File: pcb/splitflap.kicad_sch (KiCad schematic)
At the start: 37 parts, among them J1 Motor A, J10 Hall C, J11 Hall-D, J2 Motor B, J3 Motor C, J4 Motor D, J7 Barrel_Jack_Switch, J8 Hall A, J9 Hall B, SW1 A, SW2 B, SW3 IO0, SW4 RST, U1 ULN2003, U12 LM2596S-5, U2 ULN2003, U3 ESP32-DevKitC, U4 ULN2003

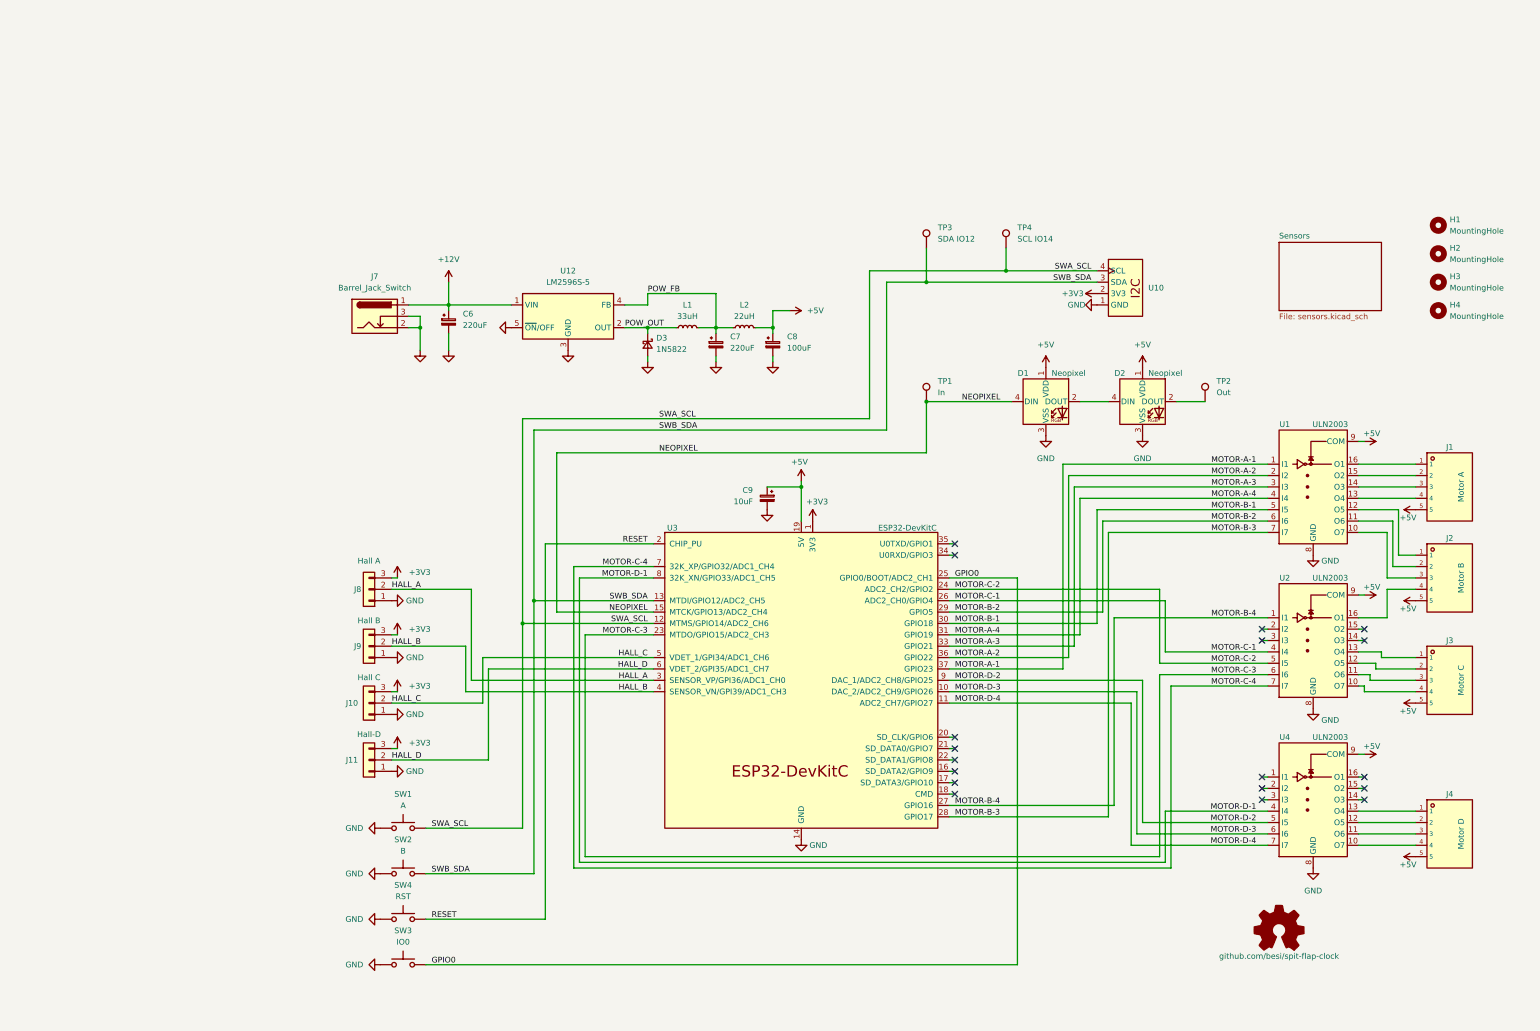
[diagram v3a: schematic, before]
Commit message: Rework 6
Added power flags to external power inputs. Fixed Motor connector pins from Unspecified to Passive, per KiCad fashion. Made the ERC pass without exclusions.

Added power decoupling to Hall sensor connectors and to the Neopixels.

Moved the IN test point for better probing accessibility. Test points use teardrop connections for integrity in face of probing.

Added a ground clip area for scope probes etc.

Added a 3D model of the pushbuttons.
Rework 6

Change revision to 1.2.
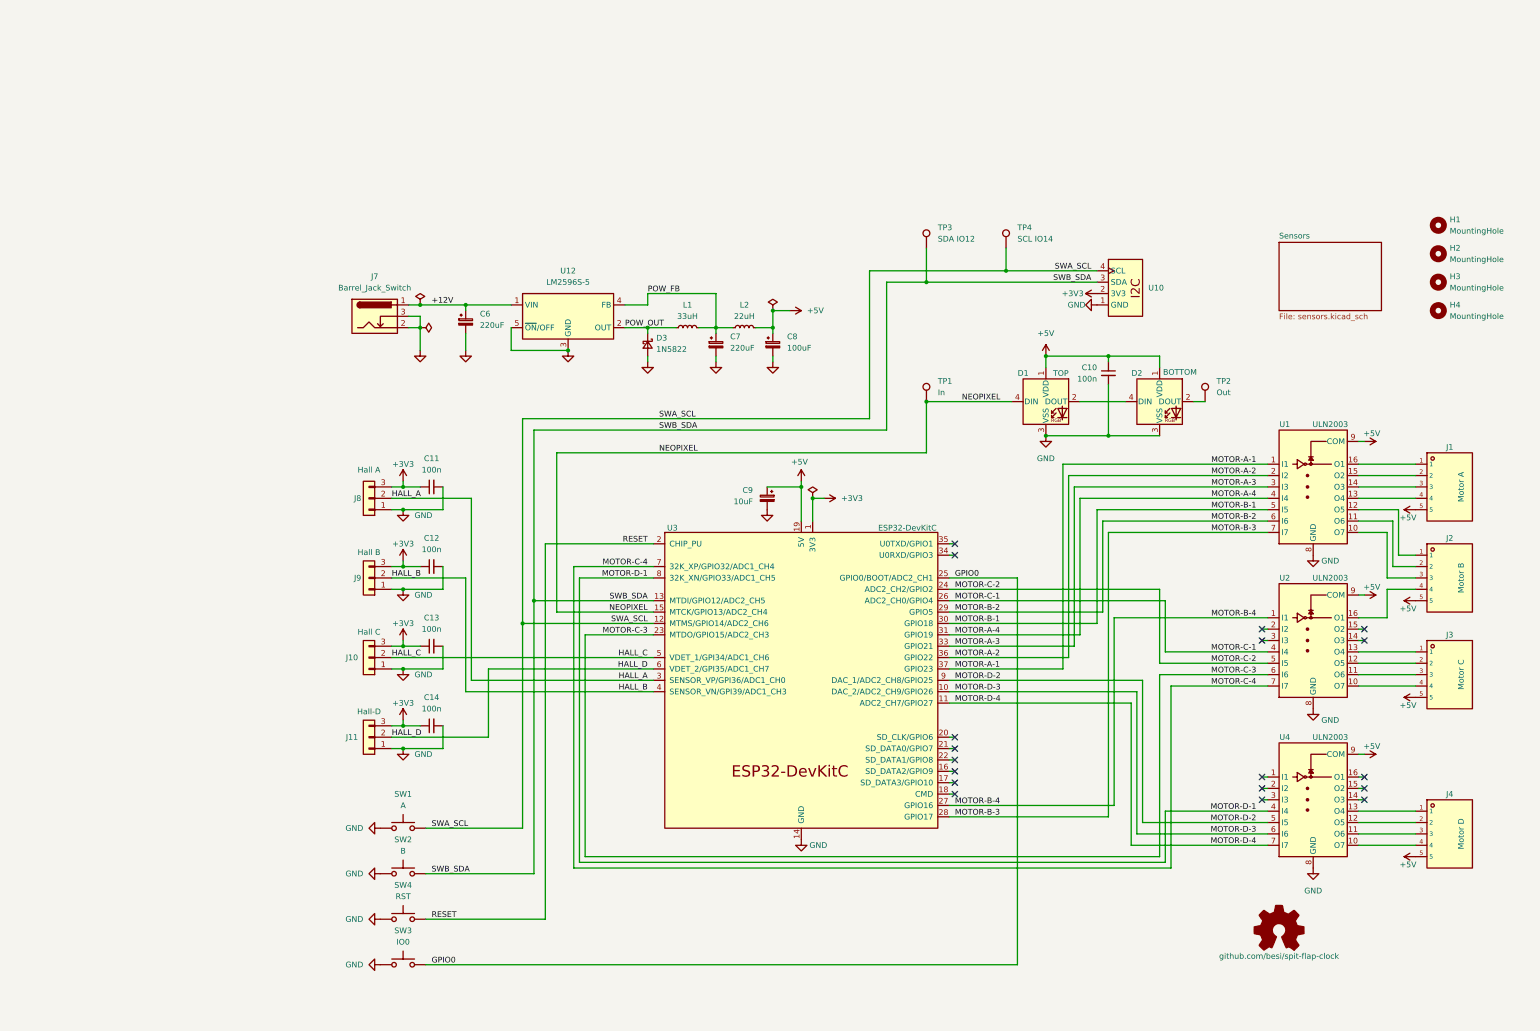
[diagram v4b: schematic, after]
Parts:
- added C10, C11, C12, C13, C14: 100n, Capacitor_SMD:C_0805_2012Metric_Pad1.18x1.45mm_HandSolder, symbol Device:C_Small
- D1: Label (none) -> TOP
- D2: Label (none) -> BOTTOM
- J1, J2, J3, J4: symbol B5B-XH-A_(LF)(SN):B5B-XH-A_(LF)(SN) -> jlc_symbols:B5B-XH-A_(LF)(SN)
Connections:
- net +3V3: now also C11.1, C12.1, C13.1, C14.1
- net +5V: now also C10.1
- net GND: now also C10.2, C11.2, C12.2, C13.2, C14.2
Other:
- moved on the sheet: C6, D2, J10, J11, J3, J8, J9

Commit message: Draft of v2 board to be imported in Fusion360
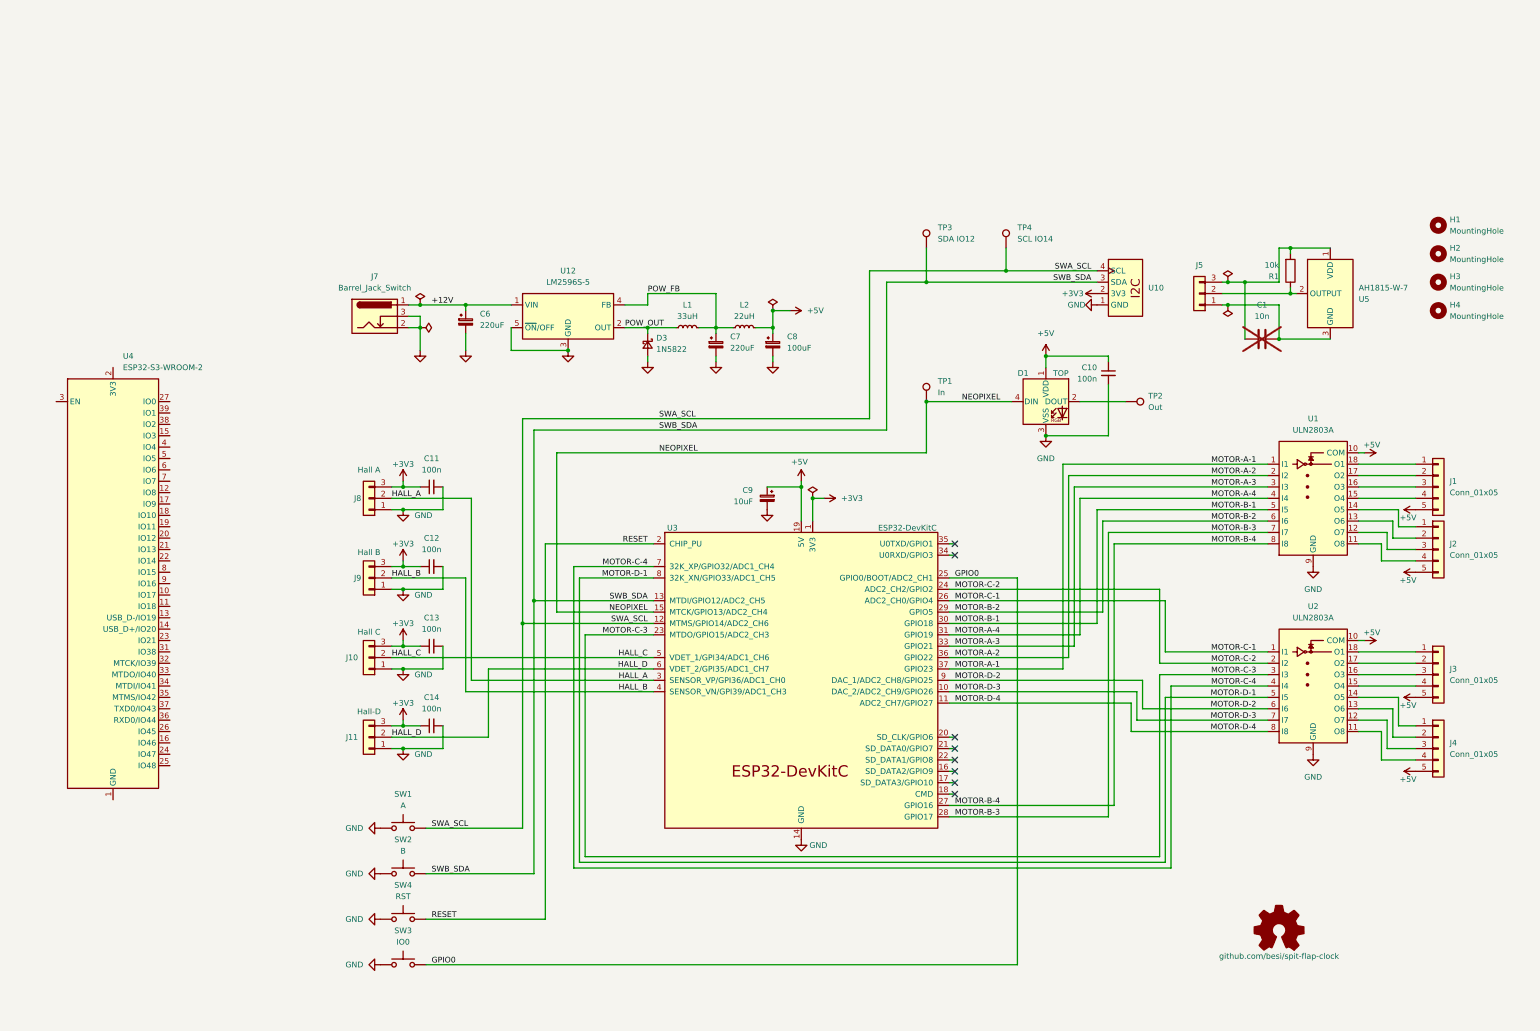
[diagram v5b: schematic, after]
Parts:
- removed D2: Neopixel, LED_SMD:LED_WS2812B_PLCC4_5.0x5.0mm_P3.2mm, symbol LED:WS2812B
- removed J1: Motor A, jlc_footprints:CONN-TH_B5B-XH-A-LF-SN, symbol jlc_symbols:B5B-XH-A_(LF)(SN)
- removed J2: Motor B, jlc_footprints:CONN-TH_B5B-XH-A-LF-SN, symbol jlc_symbols:B5B-XH-A_(LF)(SN)
- removed J3: Motor C, jlc_footprints:CONN-TH_B5B-XH-A-LF-SN, symbol jlc_symbols:B5B-XH-A_(LF)(SN)
- removed J4: Motor D, jlc_footprints:CONN-TH_B5B-XH-A-LF-SN, symbol jlc_symbols:B5B-XH-A_(LF)(SN)
- removed U1, U2, U4: ULN2003, Package_SO:SOIC-16_3.9x9.9mm_P1.27mm, symbol Transistor_Array:ULN2003
- added C1: 10n, symbol Device:C
- added J1, J2, J3, J4: Conn_01x05, Connector_JST:JST_XH_B5B-XH-A_1x05_P2.50mm_Vertical, symbol Connector_Generic:Conn_01x05
- added J5: Conn_01x03, Connector_PinHeader_2.54mm:PinHeader_1x03_P2.54mm_Vertical, symbol Connector_Generic:Conn_01x03
- added R1: 10k, Resistor_SMD:R_0805_2012Metric_Pad1.20x1.40mm_HandSolder, symbol Device:R
- added U1, U2: ULN2803A, Package_SO:SOP-18_7.495x11.515mm_P1.27mm, symbol Transistor_Array:ULN2803A
- added U4: ESP32-S3-WROOM-2, RF_Module:ESP32-S3-WROOM-2, symbol RF_Module:ESP32-S3-WROOM-2
- added U5: AH1815-W-7, Package_TO_SOT_SMD:SC-59_Handsoldering, symbol Sensor_Magnetic:AH1806-W
- J10, J11, J8, J9: footprint Connector_JST:JST_EH_B3B-EH-A_1x03_P2.50mm_Vertical -> Connector_JST:JST_XH_B3B-XH-A_1x03_P2.50mm_Vertical
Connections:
- net +5V: now also J1.5 (Pin_5), J2.5 (Pin_5), J3.5 (Pin_5), J4.5 (Pin_5), U1.10 (COM), U2.10 (COM)
- net GND: now also U1.9 (GND), U2.9 (GND)
- net MOTOR-A-1: now also U1.1 (I1)
- net MOTOR-A-2: now also U1.2 (I2)
- net MOTOR-A-3: now also U1.3 (I3)
- net MOTOR-A-4: now also U1.4 (I4)
- net MOTOR-B-1: now also U1.5 (I5)
- net MOTOR-B-2: now also U1.6 (I6)
- net MOTOR-B-3: now also U1.7 (I7)
- net MOTOR-B-4: now also U1.8 (I8)
- net MOTOR-C-1: now also U2.1 (I1)
- net MOTOR-C-2: now also U2.2 (I2)
- net MOTOR-C-3: now also U2.3 (I3)
- net MOTOR-C-4: now also U2.4 (I4)
- net MOTOR-D-1: now also U2.5 (I5)
- net MOTOR-D-2: now also U2.6 (I6)
- net MOTOR-D-3: now also U2.7 (I7)
- net MOTOR-D-4: now also U2.8 (I8)
- net at TP2.1: now also D1.2 (DOUT)
- new net: C1.1, J5.3 (Pin_3), R1.2, U5.1 (VDD)
- new net: J5.2 (Pin_2), R1.1, U5.2 (OUTPUT)
- new net: C1.2, J5.1 (Pin_1), U5.3 (GND)
- new net: J4.4 (Pin_4), U2.11 (O8)
- new net: J4.3 (Pin_3), U2.12 (O7)
- new net: J4.2 (Pin_2), U2.13 (O6)
- new net: J4.1 (Pin_1), U2.14 (O5)
- new net: J3.4 (Pin_4), U2.15 (O4)
- new net: J3.3 (Pin_3), U2.16 (O3)
- new net: J3.2 (Pin_2), U2.17 (O2)
- new net: J3.1 (Pin_1), U2.18 (O1)
- new net: J2.4 (Pin_4), U1.11 (O8)
- new net: J2.3 (Pin_3), U1.12 (O7)
- new net: J2.2 (Pin_2), U1.13 (O6)
- new net: J2.1 (Pin_1), U1.14 (O5)
- new net: J1.4 (Pin_4), U1.15 (O4)
- new net: J1.3 (Pin_3), U1.16 (O3)
- new net: J1.2 (Pin_2), U1.17 (O2)
- new net: J1.1 (Pin_1), U1.18 (O1)
- new net: U4.1 (GND), U4.40 (GND), U4.41 (GND)
- no-connect marks 18 -> 8
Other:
- removed sheet Sensors
- moved on the sheet: TP2

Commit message: V2 WIP
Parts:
- removed C7: 220uF, Capacitor_THT:CP_Radial_D10.0mm_P3.50mm, symbol Device:C_Polarized_Small
- removed D1: Neopixel, LED_SMD:LED_WS2812B_PLCC4_5.0x5.0mm_P3.2mm, symbol LED:WS2812B
- removed J5: Conn_01x03, Connector_PinHeader_2.54mm:PinHeader_1x03_P2.54mm_Vertical, symbol Connector_Generic:Conn_01x03
- removed TP1: In, TestPoint:TestPoint_Pad_D1.5mm, symbol Connector:TestPoint
- removed TP2: Out, TestPoint:TestPoint_Pad_D1.5mm, symbol Connector:TestPoint
- removed TP3: SDA IO12, TestPoint:TestPoint_Pad_D1.5mm, symbol Connector:TestPoint
- removed TP4: SCL IO14, TestPoint:TestPoint_Pad_D1.5mm, symbol Connector:TestPoint
- removed U3: ESP32-DevKitC, PCM_Espressif:ESP32-DevKitC, symbol espsbeat:ESP32-DevKitC
- added C15, C7: 100n, Capacitor_SMD:C_0805_2012Metric_Pad1.18x1.45mm_HandSolder, symbol Device:C_Small
- added C16, C3: 10u @ 16V, Capacitor_SMD:CP_Elec_4x5.7, symbol Device:C_Polarized_Small
- added C18: 1u, Capacitor_SMD:C_0805_2012Metric_Pad1.18x1.45mm_HandSolder, symbol Device:C_Small
- added C2, C4: 100uF, Capacitor_SMD:CP_Elec_5x5.3, symbol Device:C_Polarized_Small
- added C5: 220uF, Capacitor_SMD:CP_Elec_8x11.9, symbol Device:C_Polarized_Small
- added D1: SK6812MINI, LED_SMD:LED_SK6812MINI_PLCC4_3.5x3.5mm_P1.75mm, symbol LED:SK6812MINI
- added J5: Barrel_Jack_Switch, pj-060a:pj-060a, symbol Connector:Barrel_Jack_Switch
- added J6: USB_C_Receptacle_USB2.0_16P, Connector_USB:USB_C_Receptacle_GCT_USB4105-xx-A_16P_TopMnt_Horizontal, symbol Connector:USB_C_Receptacle_USB2.0_16P
- added M1: ~, 28byj:28byj, symbol 28byj:28byj
- added R2, R3: 5k1, Resistor_SMD:R_0603_1608Metric, symbol Device:R_Small
- added R4: 10k, Resistor_SMD:R_0603_1608Metric_Pad0.98x0.95mm_HandSolder, symbol Device:R
- added U3: DS18B20, Package_TO_SOT_THT:TO-92_Inline_Wide, symbol Sensor_Temperature:DS18B20
- added U6: UART, Connector_PinHeader_2.54mm:PinHeader_1x04_P2.54mm_Vertical, symbol ftdi-connector:TTL
- added U7: LD1117S33CTR, Package_TO_SOT_SMD:SOT-223-3_TabPin2, symbol Regulator_Linear:LD1117S33TR_SOT223
- added U8: DCF-77, dcf77:dcf77, symbol dcf77:dcf77
- C1: now fitted
- C10, C11, C12, C13, C14, J1, J2, J3, J4, J7, R1, U1, U2, U5: MPN (none) -> (none)
- C6: footprint Capacitor_THT:CP_Radial_D10.0mm_P3.50mm -> Capacitor_SMD:CP_Elec_8x11.9; MPN (none) -> A768KS227M1VLAE024
- C8: value 100uF -> 10u @ 16V; footprint Capacitor_THT:CP_Radial_D10.0mm_P3.50mm -> Capacitor_SMD:CP_Elec_4x5.7; MPN (none) -> 865080340001
- C9: value 10uF -> 10u @ 16V; footprint Capacitor_THT:CP_Radial_D5.0mm_P2.00mm -> Capacitor_SMD:CP_Elec_4x5.7; MPN (none) -> 865080340001
- D3: MPN (none) -> 1N5822
- H1, H2, H3, H4, OSHW1: MPN (none) -> (none); now not fitted
- J10, J11, J9: footprint Connector_JST:JST_XH_B3B-XH-A_1x03_P2.50mm_Vertical -> Connector_JST:JST_PH_B3B-PH-K_1x03_P2.00mm_Vertical; MPN (none) -> (none)
- J8: footprint Connector_JST:JST_XH_B3B-XH-A_1x03_P2.50mm_Vertical -> Connector_JST:JST_PH_B3B-PH-K_1x03_P2.00mm_Vertical
- L1: footprint Inductor_THT:L_Radial_D7.2mm_P3.00mm_Murata_1700 -> Inductor_SMD:L_APV_ANR6028; MPN (none) -> NR6028T330M
- L2: footprint Inductor_THT:L_Radial_D7.2mm_P3.00mm_Murata_1700 -> Inductor_SMD:L_APV_ANR5045; MPN (none) -> TYS5040220M-10
- SW1, SW2, SW4: MPN (none) -> 434133025816
- SW3: value IO0 -> Mode; MPN (none) -> 434133025816
- U10: footprint qwiic-adapter:qwiic-adapter -> Connector_JST:JST_SH_BM04B-SRSS-TB_1x04-1MP_P1.00mm_Vertical; MPN (none) -> BM04B-SRSS-TB
- U12: MPN (none) -> LM2596S-5.0
- U4: value ESP32-S3-WROOM-2 -> ESP32-S3-WROOM-1; footprint RF_Module:ESP32-S3-WROOM-2 -> RF_Module:ESP32-S3-WROOM-1; MPN (none) -> ESP32-S3-WROOM-1-N4
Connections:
- net +12V: now also J5.1
- net +3V3: now also C1.1, R1.2, U4.2 (3V3), U5.1 (VDD), C16.1, C2.1, C7.2, D1.4 (VDD), R4.2, U3.3 (V_{DD}), U6.4 (VDD), U7.2 (VO), U8.1 (VDD)
- net +5V: now also C10.2, C15.2, C3.1, C4.1, J6.A4 (VBUS), J6.A9 (VBUS), J6.B4 (VBUS), J6.B9 (VBUS), U7.3 (VI); no longer C10.1
- net GND: now also C1.2, C10.1, U4.1 (GND), U4.40 (GND), U4.41 (GND), U5.3 (GND), C15.1, C16.2, C18.1, C2.2, C3.2, C4.2, C5.2, C7.1, D1.2 (VSS), J5.2, U3.1 (GND), U6.1 (GND), U7.1 (GND), U8.2 (GND), U8.4 (~{EN}); no longer C10.2, J7.3
- net GPIO0: now also U4.27 (IO0)
- net HALL_A: now also R1.1, U4.11 (IO18), U5.2 (OUTPUT)
- net HALL_B: now also U4.25 (IO48)
- net HALL_C: now also U4.24 (IO47)
- net HALL_D: now also U4.20 (IO12)
- net MOTOR-A-1: now also U4.39 (IO1)
- net MOTOR-A-2: now also U4.38 (IO2)
- net MOTOR-A-3: now also U4.35 (MTMS/IO42)
- net MOTOR-A-4: now also U4.34 (MTDI/IO41)
- net MOTOR-B-1: now also U4.33 (MTDO/IO40)
- net MOTOR-B-2: now also U4.32 (MTCK/IO39)
- net MOTOR-B-3: now also U4.31 (IO38)
- net MOTOR-B-4: now also U4.6 (IO6)
- net MOTOR-C-1: now also U4.21 (IO13)
- net MOTOR-C-2: now also U4.22 (IO14)
- net MOTOR-C-3: now also U4.23 (IO21)
- net MOTOR-C-4: now also U4.19 (IO11)
- net MOTOR-D-1: now also U4.18 (IO10)
- net MOTOR-D-2: now also U4.17 (IO9)
- net MOTOR-D-3: now also U4.15 (IO3)
- net MOTOR-D-4: now also U4.12 (IO8)
- net POW_FB: now also C5.1
- net RESET: now also U4.3 (EN), C18.2, R4.1
- net SWA_SCL: now also U4.10 (IO17)
- net SWB_SDA: now also U4.9 (IO16)
- net MOUT-D4: now reaches J4.4 (Pin_4), U2.11 (O8)
- net MOUT-D3: now reaches J4.3 (Pin_3), U2.12 (O7)
- net MOUT-D2: now reaches J4.2 (Pin_2), U2.13 (O6)
- net MOUT-D1: now reaches J4.1 (Pin_1), U2.14 (O5)
- net MOUT-C4: now reaches J3.4 (Pin_4), U2.15 (O4)
- net MOUT-C3: now reaches J3.3 (Pin_3), U2.16 (O3)
- net MOUT-C2: now reaches J3.2 (Pin_2), U2.17 (O2)
- net MOUT-C1: now reaches J3.1 (Pin_1), U2.18 (O1)
- net MOUT-B4: now reaches J2.4 (Pin_4), U1.11 (O8)
- net MOUT-B3: now reaches J2.3 (Pin_3), U1.12 (O7)
- net MOUT-B2: now reaches J2.2 (Pin_2), U1.13 (O6)
- net MOUT-B1: now reaches J2.1 (Pin_1), U1.14 (O5)
- net MOUT-A4: now reaches J1.4 (Pin_4), U1.15 (O4)
- net MOUT-A3: now reaches J1.3 (Pin_3), U1.16 (O3)
- net MOUT-A2: now reaches J1.2 (Pin_2), U1.17 (O2)
- net MOUT-A1: now reaches J1.1 (Pin_1), U1.18 (O1)
- net USB_N: now reaches U4.13 (USB_D-/IO19)
- net USB_N: now also J6.A7 (D-), J6.B7 (D-)
- net USB_P: now reaches U4.14 (USB_D+/IO20)
- net USB_P: now also J6.A6 (D+), J6.B6 (D+)
- net RX: now reaches U4.36 (RXD0/IO44)
- net RX: now also U6.3 (TX)
- net TX: now reaches U4.37 (TXD0/IO43)
- net TX: now also U6.2 (RX)
- net DCF77: now reaches U4.4 (IO4)
- net DCF77: now also U8.3 (OUT)
- net TEMP: now reaches U4.5 (IO5)
- net TEMP: now also U3.2 (DQ)
- net Neopixel: now reaches U4.8 (IO15)
- net Neopixel: now also D1.3 (DIN)
- new net: J6.A5 (CC1), R3.1
- new net: J6.B5 (CC2), R2.1
- new net GNDA: J5.3, J6.A1 (GND), J6.A12 (GND), J6.B1 (GND), J6.B12 (GND), J6.S1 (SHIELD), J7.3, R2.2, R3.2
- no-connect marks 8 -> 5
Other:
- moved on the sheet: C6, D3, J1, J2, J3, J4, J7, L1, L2, U12, U4

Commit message: Cleanup libraries
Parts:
- removed U10: ~, Connector_JST:JST_SH_BM04B-SRSS-TB_1x04-1MP_P1.00mm_Vertical, symbol qwiic-adapter:qwiic-adapter
- added J12: I2C, Connector_JST:JST_SH_BM04B-SRSS-TB_1x04-1MP_P1.00mm_Vertical, symbol Connector_Generic:Conn_01x04
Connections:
- net +3V3: now also J12.2 (Pin_2)
- net GND: now also J12.1 (Pin_1)
- net SWA_SCL: now also J12.4 (Pin_4)
- net SWB_SDA: now also J12.3 (Pin_3)
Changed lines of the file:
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@@
 	)
 	(symbol
-		(lib_id "qwiic-adapter:qwiic-adapter")
-		(at 198.12 30.48 0)
-		(unit 1)
-		(exclude_from_sim no)
-		(in_bom yes)
-		(on_board yes)
-		(dnp no)
-		(fields_autoplaced yes)
-		(property "Reference" "U10"
-			(at 203.2 30.48 0)
-			(effects
-				(font
-					(size 1.27 1.27)
-				)
-				(justify left)
-			)
-		)
-		(property "Value" "~"
-			(at 196.85 30.48 0)
-			(effects
-				(font
-					(size 1.27 1.27)
-				)
-			)
-		)
-		(property "Footprint" "Connector_JST:JST_SH_BM04B-SRSS-TB_1x04-1MP_P1.00mm_Vertical"
-			(at 196.85 39.37 0)
-			(effects
-				(font
-					(size 1.27 1.27)
-				)
-				(hide yes)
-			)
-		)
-		(property "Datasheet" "https://www.digikey.com/en/products/detail/jst-sales-america-inc/BM04B-SRSS-TB/926696"
-			(at 196.85 30.48 0)
-			(effects
-				(font
-					(size 1.27 1.27)
-				)
-				(hide yes)
-			)
-		)
-		(property "Description" ""
-			(at 198.12 30.48 0)
-			(effects
-				(font
-					(size 1.27 1.27)
-				)
-				(hide yes)
-			)
-		)
-		(property "MPN" "BM04B-SRSS-TB"
-			(at 198.12 30.48 0)
-			(effects
-				(font
-					(size 1.27 1.27)
-				)
-				(hide yes)
-			)
-		)
-		(pin "2"
-		)
-		(pin "4"
-		)
-		(pin "3"
-		)
-		(pin "1"
-		)
-		(instances
-			(project "splitflap"
-				(path "/f3b5a3df-7272-4af1-9be6-6c38555ab067"
-					(reference "U10")
-					(unit 1)
-				)
-			)
-		)
-	)
-	(symbol
 		(lib_id "power:GND")
 		(at 219.71 34.29 0)
@@
 					(unit 1)
 				)
+			)
+		)
+	)
+	(symbol
+		(lib_id "Connector_Generic:Conn_01x04")
+		(at 196.85 31.75 0)
+		(mirror x)
+		(unit 1)
+		(exclude_from_sim no)
+		(in_bom yes)
+		(on_board yes)
+		(dnp no)
+		(fields_autoplaced yes)
+		(property "Reference" "J12"
+			(at 196.85 20.32 0)
+			(effects
+				(font
+					(size 1.27 1.27)
+				)
+			)
+		)
+		(property "Value" "I2C"
+			(at 196.85 22.86 0)
+			(effects
+				(font
+					(size 1.27 1.27)
+				)
+			)
+		)
+		(property "Footprint" "Connector_JST:JST_SH_BM04B-SRSS-TB_1x04-1MP_P1.00mm_Vertical"
+			(at 196.85 31.75 0)
+			(effects
+				(font
+					(size 1.27 1.27)
+				)
+				(hide yes)
+			)
+		)
+		(property "Datasheet" "~"
+			(at 196.85 31.75 0)
+			(effects
+				(font
+					(size 1.27 1.27)
+				)
+				(hide yes)
+			)
+		)
+		(property "Description" "Generic connector, single row, 01x04, script generated (kicad-library-utils/schlib/autogen/connector/)"
+			(at 196.85 31.75 0)
+			(effects
+				(font
+					(size 1.27 1.27)
+				)
+				(hide yes)
+			)
+		)
+		(pin "3"
+		)
+		(pin "2"
+		)
+		(pin "1"
+		)
+		(pin "4"
+		)
+		(instances
+			(project ""
+				(path "/f3b5a3df-7272-4af1-9be6-6c38555ab067"
+					(reference "J12")
+					(unit 1)
+				)
